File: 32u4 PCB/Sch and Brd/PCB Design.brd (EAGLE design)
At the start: 71.6 x 74.8 mm, 53 parts, among them J1 AVR_SPI_PROG_3X2PTH, J2 AMP FCI 10103594-0001LF, Q1 16MHz, U1 ATMEGA32U4-AU

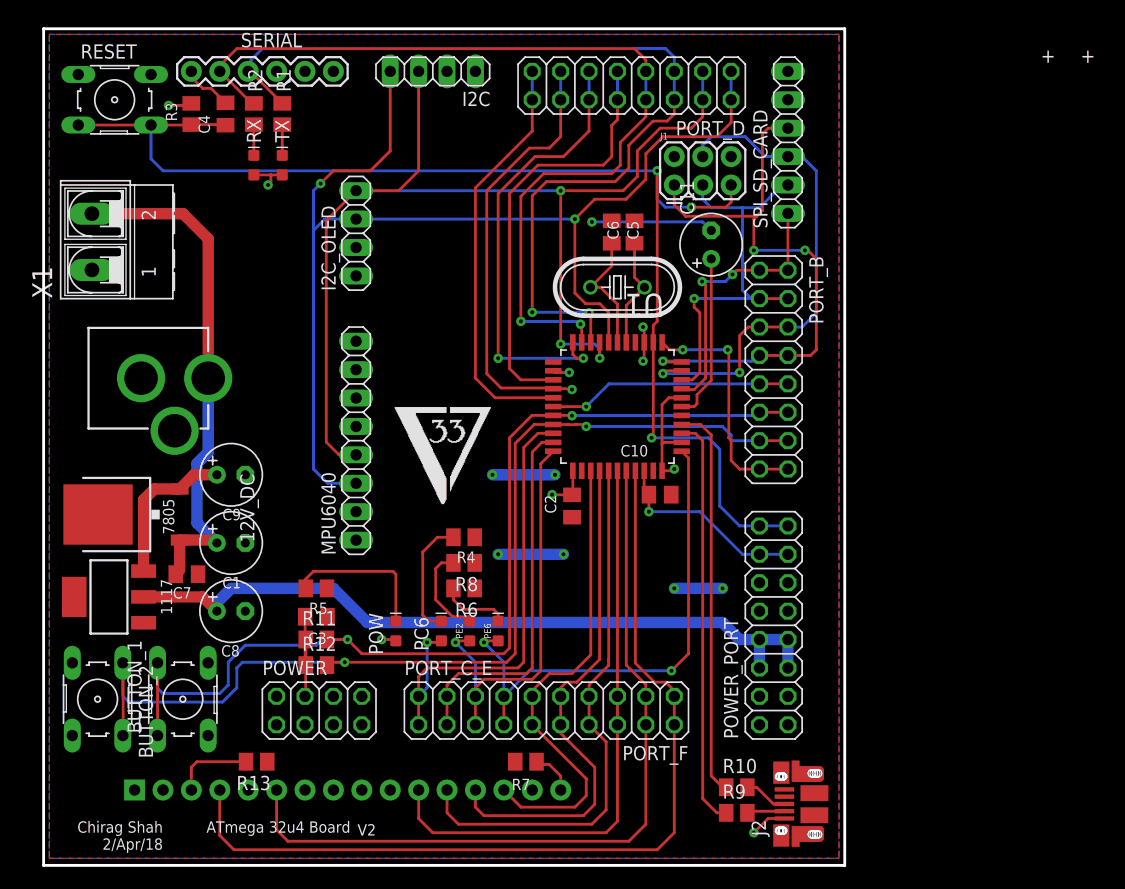
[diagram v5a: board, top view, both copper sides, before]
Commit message: Adjusted Silkscreen, added bluetooth
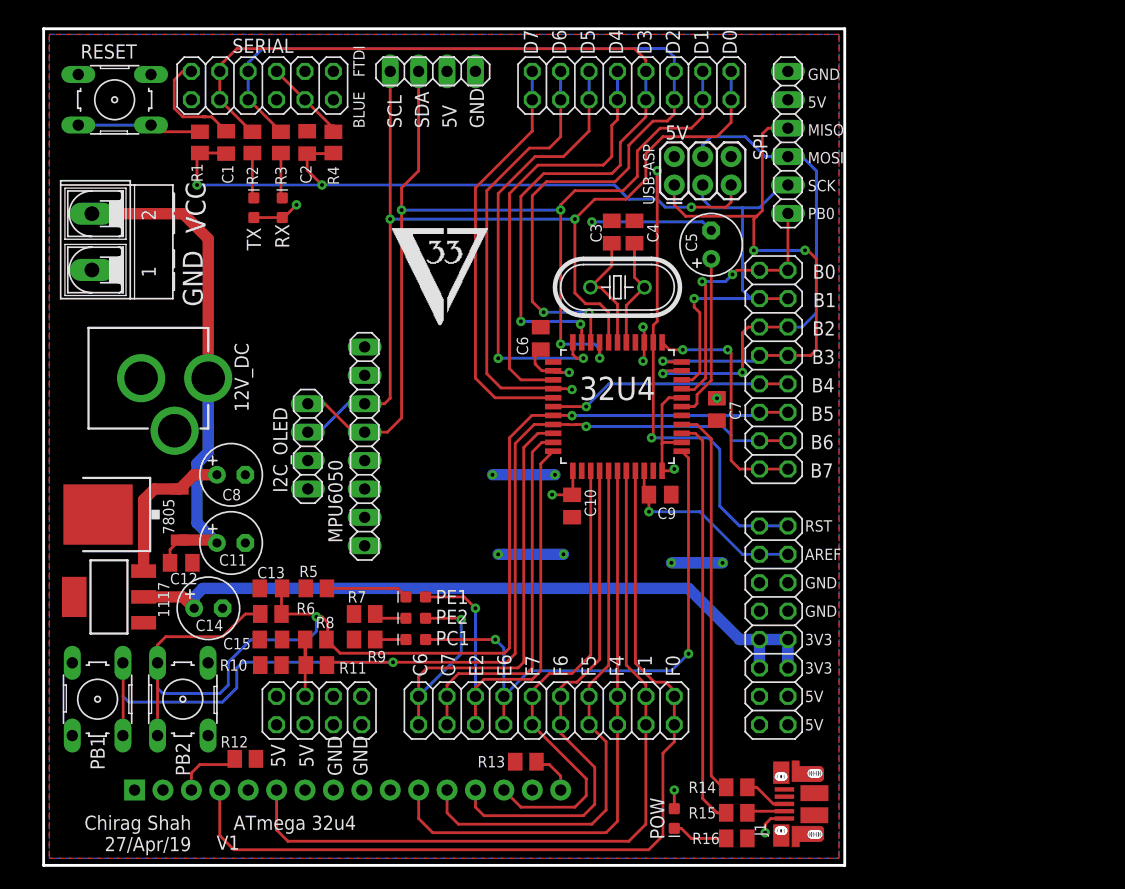
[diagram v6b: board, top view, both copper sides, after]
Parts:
- removed J2: AMP FCI 10103594-0001LF, SparkFun-Connectors:USB-MICROB-PTH
- removed MPU6040: (no value), pinhead:1X08
- removed PC6, PE6: Yellow, SparkFun-LED:LED-0603
- added C12: .1uf, rcl:C0805K
- added C13, C15: .1uF, rcl:C0805K
- added C14: 10uf, resistor:E2,5-6
- added MPU6050: (no value), pinhead:1X08
- added PC1, PE1: Yellow, SparkFun-LED:LED-0603
- added R14, R15: 22, resistor:M0805
- added R16: 330, resistor:M0805
- added USB-ASP: AVR_SPI_PROG_3X2PTH, SparkFun-Connectors:2X3
- C1: value 10uf -> 0.33µF; device resistor:E2,5-6 -> rcl:C0805K
- C11: value 1uF -> 10uf
- C3: value .1uF -> 22pF
- C4: value 0.33µF -> 22pF
- C5: value 22pF -> 1uF; device rcl:C0805K -> resistor:E2,5-6
- C6: value 22pF -> .1uF
- C7: value .1uf -> .1uF
- C9: value 10uf -> .1uF; device resistor:E2,5-6 -> rcl:C0805K
- J1: value AVR_SPI_PROG_3X2PTH -> AMP FCI 10103594-0001LF; device SparkFun-Connectors:2X3 -> SparkFun-Connectors:USB-MICROB-PTH
- R1: value 1K -> 330
- R10, R9: value 22 -> 330
- R12: value 10K -> 4k7
- R13: value 4k7 -> 220
- R3: value 10k -> 1K
- R4: value 330 -> 10k
- R7: value 220 -> 330
- R8: value 330 -> 10K
- SERIAL: value 6_PIN_SERIAL_CABLEPTH -> (none); device SparkFun-Connectors:FTDI_BASIC -> pinhead:2X06
- moved J1 56.5 mm to (74.9, 1.02), turned to 90 degrees
- moved C11 50.5 mm to (24.1, 24.4), turned to 0 degrees
- moved C7 49.6 mm to (67.6, 36.3), turned to 270 degrees
- moved C3 43.4 mm to (58.2, 52.2), turned to 270 degrees
- moved R10 43.1 mm to (27.7, 13.5)
- moved C2 40.2 mm to (30.9, 60.2), turned to 90 degrees
- moved C9 38.4 mm to (62.5, 28.7)
- moved C4 38.1 mm to (60.2, 52.2), turned to 270 degrees
- moved R4 37.2 mm to (33.3, 60.2), turned to 270 degrees
- moved R9 36.7 mm to (36.1, 15.7)
- moved C1 35.8 mm to (23.7, 60.2), turned to 90 degrees
- moved POW 30.0 mm to (63.8, -0.25), turned to 270 degrees
- moved R13 24.1 mm to (50.5, 4.83), turned to 0 degrees
- moved R7 19.6 mm to (36.1, 18.0)
- moved I2C_OLED 19.5 mm to (31.0, 33.0)
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- renumbered BUTTON_1 to PB2, BUTTON_2 to PB1, SPI_SD_CARD to SPI, U1 to 32U4
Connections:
- new net EN: SERIAL.2
- new net N$10: R1.2, RESET.3, RESET.4
- new net N$11: PB1.1, PB1.2, R10.1
- new net N$12: PB2.1, PB2.2, R6.1
- new net STATE: SERIAL.12
- net +12V: now also C11.+, C12.1; no longer C1.+, C7.1
- net +5V: now also C10.1, C6.1, C7.1, C8.+, J1.VBUS, MPU6050.1, R4.1, R8.1, SERIAL.4, SERIAL.5, USB-ASP.2; no longer C2.1, C3.1, C9.+, J1.2, J2.VBUS, MPU6040.1, R12.1, R3.1, SERIAL.VCC
- net 3V3: now also C14.+; no longer C8.+
- net AD0: now also MPU6050.7; no longer MPU6040.7
- net AREF: now also C9.1; no longer C10.1
- net CTS: now also SERIAL.3; no longer SERIAL.CTS
- net D+: now also J1.D+, R14.2; no longer J2.D+, R10.2
- net D-: now also J1.D-, R15.2; no longer J2.D-, R9.2
- net DTR: now also C1.2, SERIAL.11; no longer C4.2, SERIAL.DTR
- net GND: now also C12.2, C13.2, C14.-, C15.2, C3.1, C4.1, C5.-, C6.2, C9.2, J1.GND, MPU6050.2, R12.1, R16.1, R9.1, SERIAL.1, SERIAL.6, USB-ASP.6; no longer C1.-, C3.2, C5.1, C6.1, C9.-, J1.6, J2.GND, MPU6040.2, R4.1, R6.1, R8.1, SERIAL.GND
- net ID: now also J1.ID; no longer J2.ID
- net INT: now also MPU6050.8; no longer MPU6040.8
- net N$1: now also PC1.C, R7.2; no longer PC6.C, R4.2
- net N$13: now also R15.1; no longer R9.1
- net N$14: now also R13.2; no longer R7.2
- net N$15: now also R14.1; no longer R10.1
- net N$16: now also C5.+; no longer C11.+
- net N$2: now also R16.2; no longer R5.2
- net N$3: now also PE2.C, R9.2; no longer PE6.C, R6.2
- net N$6: now also R12.2; no longer R13.2
- net N$7: now also PE1.C, R5.2; no longer PE2.C, R8.2
- net N$8: now also TX.C; no longer RX.C
- net N$9: now also R3.2, RX.C; no longer R1.2, TX.C
- net PB1/SCK: now also USB-ASP.3; no longer J1.3
- net PB2/MOSI: now also USB-ASP.4; no longer J1.4
- net PB3/MISO: now also USB-ASP.1; no longer J1.1
- net PB5: now also C13.1, R6.2, R8.2; no longer PB2.1, PB2.2, R11.2
- net PB6: now also C15.1, R10.2, R11.2; no longer PB1.1, PB1.2, R12.2
- net PC6: now also PC1.A; no longer PC6.A
- net PD0/SCL: now also MPU6050.3; no longer MPU6040.3
- net PD1/SDA: now also MPU6050.4; no longer MPU6040.4
- net PD2/RXD1: now also R3.1, SERIAL.7, SERIAL.8; no longer R1.1, SERIAL.TXO
- net PD3/TXD1: now also SERIAL.10, SERIAL.9; no longer SERIAL.RXI
- net PE2: now also PE1.A; no longer PE2.A
- net PE6: now also PE2.A; no longer PE6.A
- net RESET: now also C1.1, C2.1, R1.1, R4.2, USB-ASP.5; no longer C4.1, J1.5, R3.2, RESET.3, RESET.4
- net XCL: now also MPU6050.6; no longer MPU6040.6
- net XDA: now also MPU6050.5; no longer MPU6040.5
- net XTAL1: now also C3.2; no longer C5.2
- net XTAL2: now also C4.2; no longer C6.2
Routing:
- net N$12: track 0.00 -> 18.4 mm
- net PD0/SCL: track 104.9 -> 90.8 mm
- net N$10: track 0.00 -> 11.1 mm
- net RESET: track 115.6 -> 106.5 mm, vias 3 -> 5
- net N$2: track 13.5 -> 5.01 mm
- net N$1: track 10.8 -> 2.90 mm
- net N$11: track 0.00 -> 6.54 mm
- net PE2: track 36.8 -> 42.6 mm
- net +5V: track 55.3 -> 61.1 mm
- net DTR: track 4.51 -> 10.1 mm
- net PC6: track 43.1 -> 48.3 mm
- net PB6: track 94.1 -> 88.9 mm
- net PE6: track 45.9 -> 51.0 mm
- net PD1/SDA: track 100.7 -> 95.7 mm, vias 3 -> 4
- net N$3: track 6.18 -> 2.74 mm
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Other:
- board text added: "3V3"
- board text added: "5V"
- board text added: "AREF"
- board text added: "ATmega 32u4"
- board text added: "B0"
- board text added: "B1"
- board text added: "B2"
- board text added: "B3"
- board text added: "B4"
- board text added: "B5"
- board text added: "B6"
- board text added: "B7"
- board text added: "BLUE"
- board text added: "C6"
- board text added: "C7"
- board text added: "Chirag Shah 27/Apr/19"
- board text added: "D0"
- board text added: "D1"
- board text added: "D2"
- board text added: "D3"
- board text added: "D4"
- board text added: "D5"
- board text added: "D6"
- board text added: "D7"
- board text added: "E2"
- board text added: "E6"
- board text added: "F0"
- board text added: "F1"
- board text added: "F4"
- board text added: "F5"
- board text added: "F6"
- board text added: "F7"
- board text added: "FTDI"
- board text added: "GND"
- board text added: "MISO"
- board text added: "MOSI"
- board text added: "PB0"
- board text added: "RST"
- board text added: "SCK"
- board text added: "SCL"
- board text added: "SDA"
- board text added: "V1"
- board text added: "VCC"
- board text removed: "+"
- board text removed: "ATmega 32u4 Board"
- board text removed: "Chirag Shah 2/Apr/18"
- board text removed: "V2"

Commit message: Manufacture
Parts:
- removed J1: AMP FCI 10103594-0001LF, SparkFun-Connectors:USB-MICROB-PTH
- added R17: 22, resistor:M0805
- added R18: 330, resistor:M0805
- added U1: (no value), MicroUSB:USB-MICRO-SMD
- 1117: value V_REG_LD1117VXXLD1117-SMD -> 3v3
- I2C: device pinhead:1X04 -> pinhead:2X04
- R10: value 330 -> 10K
- R11, R8: value 10K -> 330
- R12: value 4k7 -> 330
- R13: value 220 -> 10K
- R14: value 22 -> 4k7
- R15: value 22 -> 220
- R16: value 330 -> 22
- R5, R6: value 330 -> I2C
- moved R14 44.0 mm to (25.4, 5.08), turned to 180 degrees
- moved R6 40.1 mm to (42.9, 55.1), turned to 180 degrees
- moved R5 39.0 mm to (42.9, 57.7), turned to 180 degrees
- moved R13 20.6 mm to (31.8, 13.5)
- moved R15 19.4 mm to (50.5, 4.83)
- moved R12 8.69 mm to (27.7, 13.5), turned to 0 degrees
- moved R7 4.89 mm to (31.8, 20.3)
- moved R11 4.89 mm to (36.1, 15.7)
- moved R10 4.62 mm to (31.7, 15.7)
- moved R8 4.62 mm to (27.7, 18.0)
- moved R16 3.81 mm to (69.3, 1.78), turned to 0 degrees
- moved RESET 2.59 mm to (13.2, 66.5)
- moved R9 2.29 mm to (36.1, 18.0)
- moved I2C 1.27 mm to (42.2, 65.3)
- moved X1 0.80 mm to (11.4, 50.5)
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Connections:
- removed net D+: J1.D+, R14.2
- removed net D-: J1.D-, R15.2
- removed net INT: MPU6050.8
- removed net N$13: 32U4.3, R15.1
- removed net N$15: 32U4.4, R14.1
- new net D_N: 32U4.3, R17.1
- new net D_P: 32U4.4, R16.1
- new net D_USB_N: R17.2, U1.D-1
- new net D_USB_P: R16.2, U1.D+1
- net +5V: now also I2C.3, I2C.4, R10.1, R13.1, R5.1, R6.1, U1.VBUS1; no longer I2C.2, J1.VBUS, R11.1, R8.1
- net GND: now also I2C.2, R11.1, R14.1, R15.1, R18.1, U1.GND1; no longer J1.GND, R12.1, R13.1, R16.1, R5.1
- net ID: now also U1.ID1; no longer J1.ID
- net N$1: now also R9.2; no longer R7.2
- net N$11: now also R12.1; no longer R10.1
- net N$12: now also R8.1; no longer R6.1
- net N$14: now also R15.2; no longer R13.2
- net N$2: now also R18.2; no longer R16.2
- net N$3: now also R11.2; no longer R9.2
- net N$6: now also R14.2; no longer R12.2
- net N$7: now also R7.2; no longer R5.2
- net PB4: now also MPU6050.8
- net PB5: now also R10.2; no longer R6.2
- net PB6: now also R12.2, R13.2; no longer R10.2, R11.2
- net PD0/SCL: now also I2C.7, I2C.8, R5.2; no longer I2C.4
- net PD1/SDA: now also I2C.5, I2C.6, R6.2; no longer I2C.3
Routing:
- net D_N: track 0.00 -> 37.8 mm
- net D_P: track 0.00 -> 37.6 mm
- net N$13: track 36.8 -> 0.00 mm
- net N$15: track 35.1 -> 0.00 mm
- net PB4: track 21.8 -> 49.1 mm
- net PB5: track 89.2 -> 69.4 mm, vias 2 -> 1
- net N$11: track 6.54 -> 22.8 mm
- net PB6: track 88.9 -> 75.4 mm, vias 2 -> 3
- net PD0/SCL: track 90.8 -> 95.6 mm
- net +5V: track 61.1 -> 65.6 mm
- net D+: track 3.93 -> 0.00 mm
- net D-: track 3.37 -> 0.00 mm
- net D_USB_N: track 0.00 -> 3.32 mm
- net D_USB_P: track 0.00 -> 3.27 mm
- net N$10: track 11.1 -> 12.7 mm
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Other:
- board text added: "ATmega 32u4 V1"
- board text added: "Chirag Shah 16/Feb/19"
- board text removed: "ATmega 32u4"
- board text removed: "Chirag Shah 27/Apr/19"
- board text removed: "V1"
